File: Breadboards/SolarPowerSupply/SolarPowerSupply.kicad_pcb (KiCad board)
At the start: 2 copper layers, 59.9 x 34.5 mm, 49 parts, among them P101 CONN_01X04, P102 CONN_01X07, U101 bq25504, U102 TPS63051, U103 TPS63050

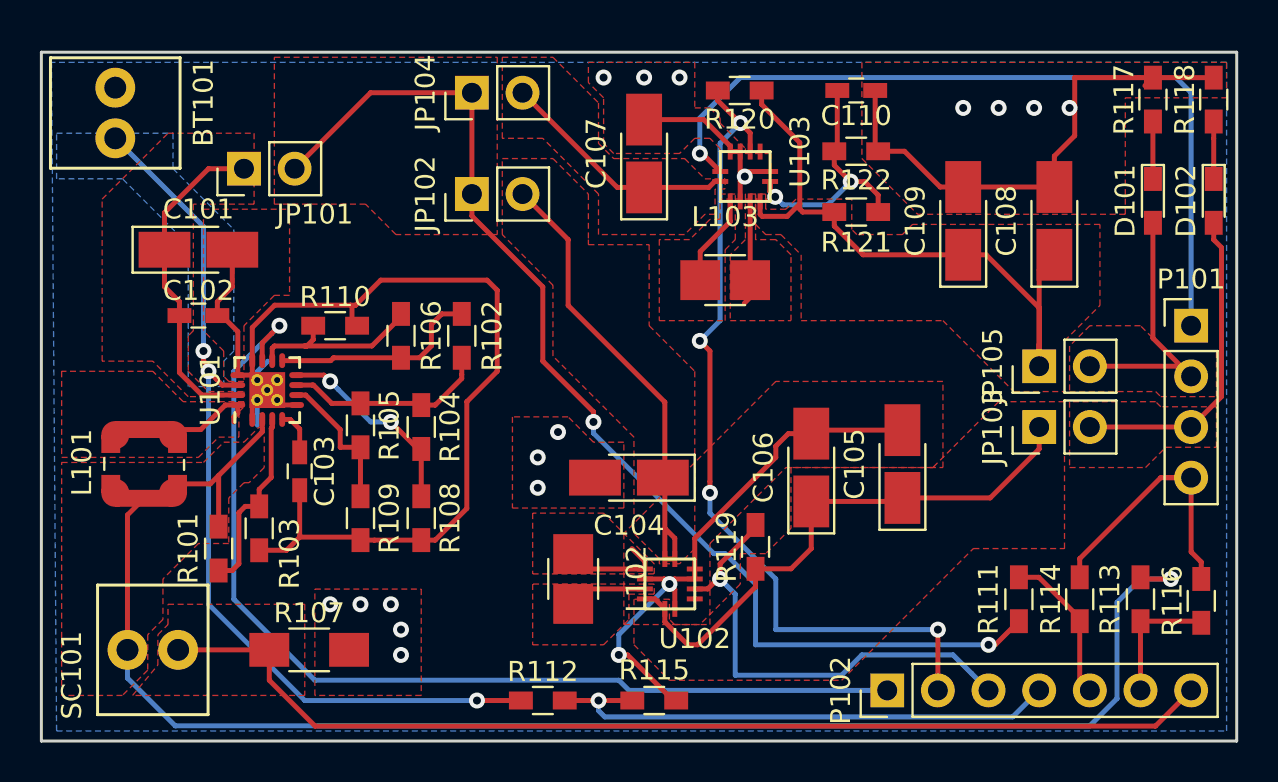
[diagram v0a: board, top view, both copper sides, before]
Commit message: Ensures Design mostly DRC clean
Removed remaining DRC errors, mostly copper traces too close.
Some DRC errors remain, within the SOIC-16 package of the bq25504,
     "PADS TOO CLOSE" -> to be ignored.
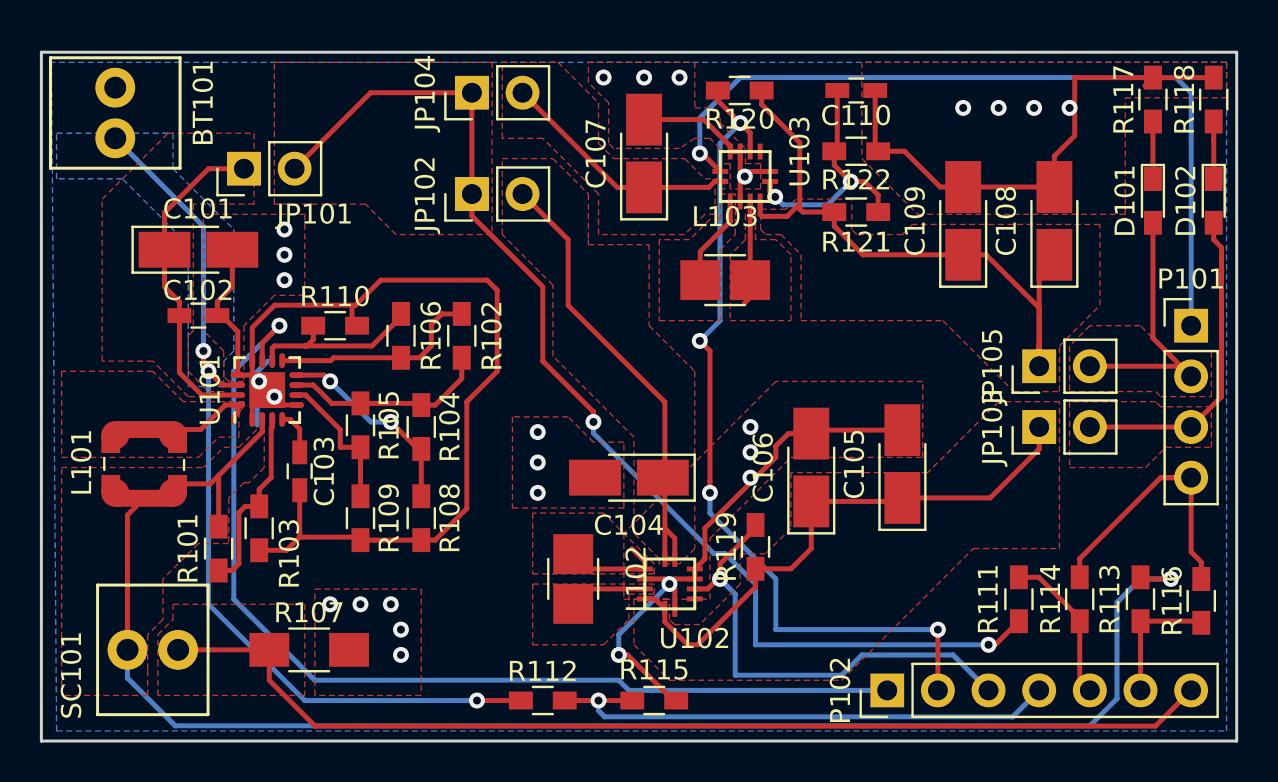
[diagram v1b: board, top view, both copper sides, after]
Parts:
- U101: footprint Housings_DFN_QFN:QFN-16-1EP_3x3mm_Pitch0.5mm_ThermalVias -> Housings_DFN_QFN:QFN-16-1EP_3x3mm_Pitch0.5mm
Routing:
- net GND: track 137.8 -> 139.5 mm, vias 18 -> 26

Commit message: Adds Octanis and Octanis-3 Logo to layout
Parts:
- added G***: LOGO, Octanis3:octanis_open_incubator_logo, B.Cu at (63.2, 111.0)
- added G***: LOGO, Octanis3:octanis3_logo, B.Cu at (83.1, 119.6)
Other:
- board text added: "SolarPowerSupply-BB Octanis-3"
